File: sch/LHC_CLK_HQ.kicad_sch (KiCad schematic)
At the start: 1 part, among them U2 Si5395

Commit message: sfp+ sheet
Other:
- company: (none) -> Karlsruhe Institute of Technology (KIT)
- title: (none) -> ATCA Simple Loopback HUB
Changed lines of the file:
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@@
 (kicad_sch (version 20230121) (generator eeschema)
   (paper "A4")
+  (title_block
+    (title "ATCA Simple Loopback HUB")
+    (date "2023-09-12")
+    (rev "1.0")
+    (company "Karlsruhe Institute of Technology (KIT)")
+    (comment 1 "Institute for Data Processing and Electronics (IPE)")
+    (comment 2 "Luis Ardila")
+    (comment 3 "IPE-380-06")
+    (comment 4 "Licensed under CERN-OHL-P-2.0")
+  )
   (bus_entry (at 208.28 100.33) (size 2.54 -2.54)
     (stroke (width 0) (type default))

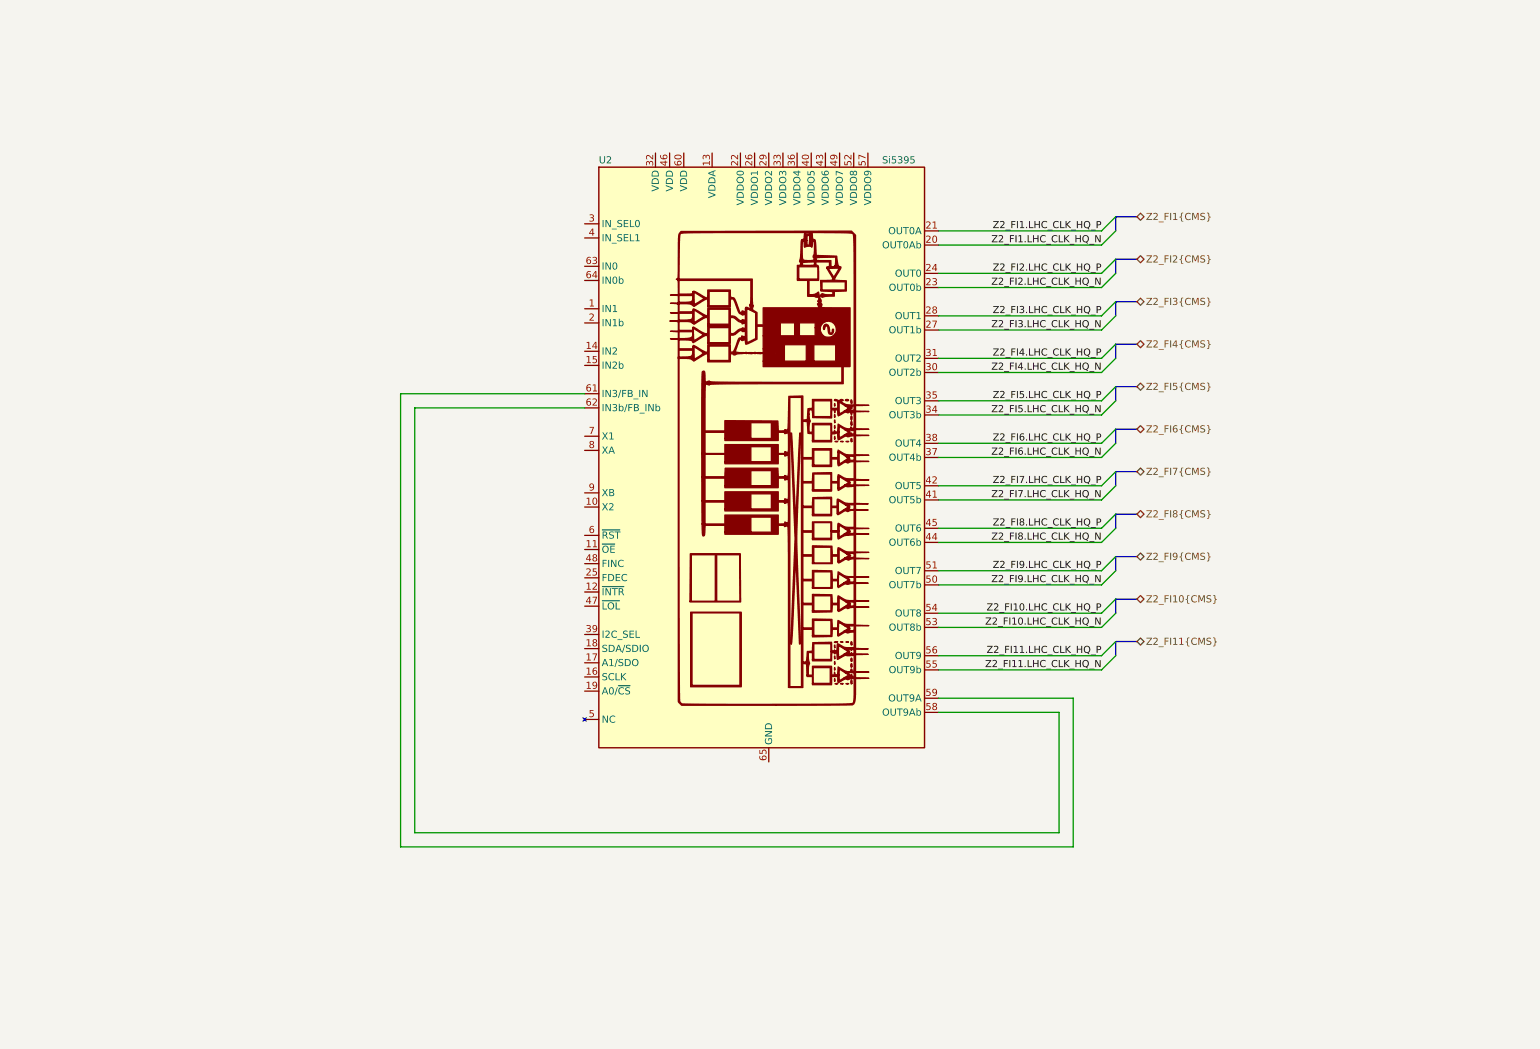
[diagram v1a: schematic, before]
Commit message: work on sc pll and pll sheet
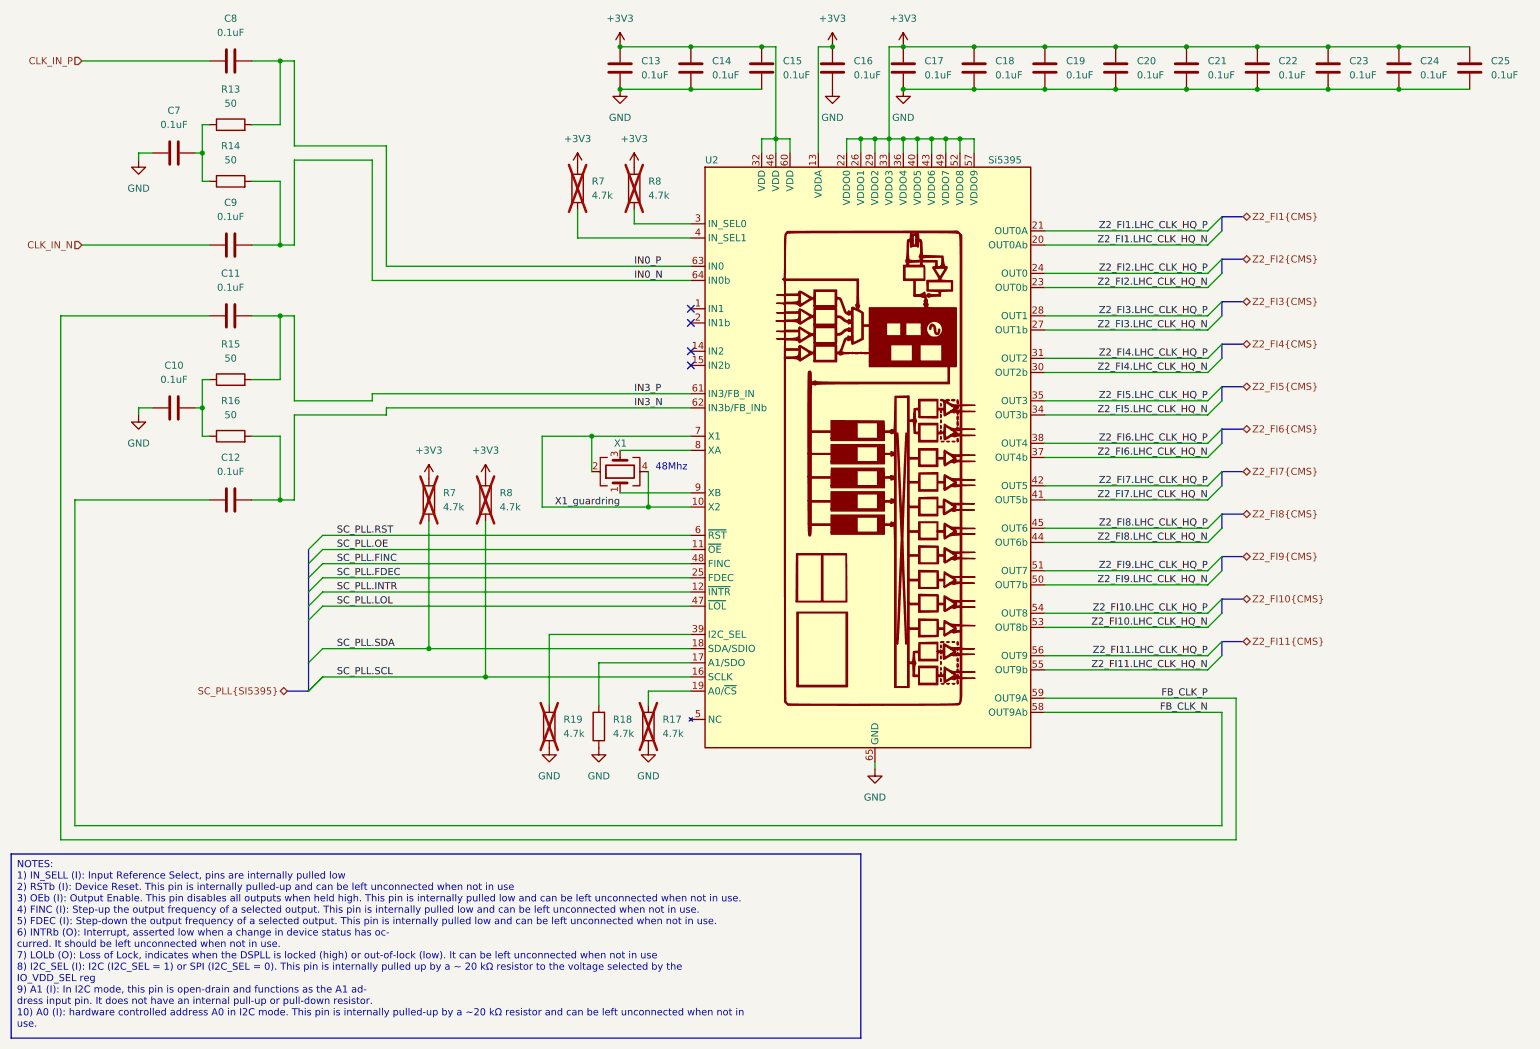
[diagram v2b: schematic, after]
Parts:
- added C10, C11, C12, C13, C14, C15, C16, C17, C18, C19, C20, C21, C22, C23, C24, C25, C7, C8, C9: 0.1uF, Capacitor_SMD:C_0402_1005Metric, symbol Device:C
- added R13, R14, R15, R16: 50, Resistor_SMD:R_0402_1005Metric, symbol Device:R
- added R17, R18, R19, R7 (x2), R8 (x2): 4.7k, Resistor_SMD:R_0402_1005Metric, symbol Device:R
- added X1: CX3225SB, Crystal:Crystal_SMD_3225-4Pin_3.2x2.5mm, symbol Device:Crystal_GND24
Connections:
- net X1_guardring: now reaches U2.10 (X2)
- net X1_guardring: now also U2.7 (X1), X1.2, X1.4
- net SC_PLL.OE: now reaches U2.11 (~{OE})
- net SC_PLL.INTR: now reaches U2.12 (~{INTR})
- net +3V3: now reaches U2.13 (VDDA)
- net +3V3: now also U2.22 (VDDO0), U2.26 (VDDO1), U2.29 (VDDO2), U2.32 (VDD), U2.33 (VDDO3), U2.36 (VDDO4), U2.40 (VDDO5), U2.43 (VDDO6), U2.46 (VDD), U2.49 (VDDO7), U2.52 (VDDO8), U2.57 (VDDO9), U2.60 (VDD), C13.2, C14.2, C15.2, C16.2, C17.2, C18.2, C19.2, C20.2, C21.2, C22.2, C23.2, C24.2, C25.2, R7.1, R7.1, R8.1, R8.1
- net SC_PLL.SCL: now reaches U2.16 (SCLK)
- net SC_PLL.SCL: now also R8.2
- net at U2.17 (A1/SDO): now also R18.2
- net SC_PLL.SDA: now reaches U2.18 (SDA/SDIO)
- net SC_PLL.SDA: now also R7.2
- net at U2.19 (A0/~{CS}): now also R17.2
- net SC_PLL.FDEC: now reaches U2.25 (FDEC)
- net at U2.3 (IN_SEL0): now also R8.2
- net at U2.39 (I2C_SEL): now also R19.2
- net at U2.4 (IN_SEL1): now also R7.2
- net SC_PLL.LOL: now reaches U2.47 (~{LOL})
- net SC_PLL.FINC: now reaches U2.48 (FINC)
- net FB_CLK_N: now reaches U2.58 (OUT9Ab)
- net FB_CLK_N: now also C12.1; no longer U2.62 (IN3b/FB_INb)
- net FB_CLK_P: now reaches U2.59 (OUT9A)
- net FB_CLK_P: now also C11.1; no longer U2.61 (IN3/FB_IN)
- net SC_PLL.RST: now reaches U2.6 (~{RST})
- net IN0_P: now reaches U2.63 (IN0)
- net IN0_P: now also C8.2, R13.2
- net IN0_N: now reaches U2.64 (IN0b)
- net IN0_N: now also C9.2, R14.2
- net GND: now reaches U2.65 (GND)
- net GND: now also C10.1, C13.1, C14.1, C15.1, C16.1, C17.1, C18.1, C19.1, C20.1, C21.1, C22.1, C23.1, C24.1, C25.1, C7.1, R17.1, R18.1, R19.1
- net at U2.8 (XA): now also X1.3
- net at U2.9 (XB): now also X1.1
- new net: C10.2, R15.1, R16.1
- new net: C7.2, R13.1, R14.1
- new net CLK_IN_N: C9.1
- new net CLK_IN_P: C8.1
- new net IN3_N: C12.2, R16.2, U2.62 (IN3b/FB_INb)
- new net IN3_P: C11.2, R15.2, U2.61 (IN3/FB_IN)
- no-connect marks 0 -> 4
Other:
- note added: "48Mhz"

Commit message: sch work
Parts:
- removed R7, R8: 4.7k, Resistor_SMD:R_0402_1005Metric, symbol Device:R
- added FB1: FerriteBead, Inductor_SMD:L_0603_1608Metric, symbol Device:FerriteBead
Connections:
- net +3V3: now also FB1.1; no longer C13.2, C14.2, C15.2, C16.2, U2.13 (VDDA), U2.32 (VDD), U2.46 (VDD), U2.60 (VDD)
- new net +1V8: C13.2, C14.2, C15.2, U2.32 (VDD), U2.46 (VDD), U2.60 (VDD)
- new net +VDDA: C16.2, FB1.2, U2.13 (VDDA)
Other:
- note added: "I2C Address = 8'b1101_001X, 8'hD2, 7'h69"

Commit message: before sch review
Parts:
- R17, R19, R7, R8: now left out of the parts list
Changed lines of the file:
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@@
   )
   (symbol (lib_id "Device:R") (at 114.3 44.45 0) (unit 1)
-    (in_bom yes) (on_board yes) (dnp yes) (fields_autoplaced)
+    (in_bom no) (on_board yes) (dnp yes) (fields_autoplaced)
     (property "Reference" "R7" (at 116.84 43.18 0)
       (effects (font (size 1.27 1.27)) (justify left))
@@
   )
   (symbol (lib_id "Device:R") (at 127 140.97 180) (unit 1)
-    (in_bom yes) (on_board yes) (dnp yes) (fields_autoplaced)
+    (in_bom no) (on_board yes) (dnp yes) (fields_autoplaced)
     (property "Reference" "R17" (at 129.54 139.7 0)
       (effects (font (size 1.27 1.27)) (justify right))
@@
   )
   (symbol (lib_id "Device:R") (at 124.46 44.45 0) (unit 1)
-    (in_bom yes) (on_board yes) (dnp yes) (fields_autoplaced)
+    (in_bom no) (on_board yes) (dnp yes) (fields_autoplaced)
     (property "Reference" "R8" (at 127 43.18 0)
       (effects (font (size 1.27 1.27)) (justify left))
@@
   )
   (symbol (lib_id "Device:R") (at 109.22 140.97 180) (unit 1)
-    (in_bom yes) (on_board yes) (dnp yes) (fields_autoplaced)
+    (in_bom no) (on_board yes) (dnp yes) (fields_autoplaced)
     (property "Reference" "R19" (at 111.76 139.7 0)
       (effects (font (size 1.27 1.27)) (justify right))

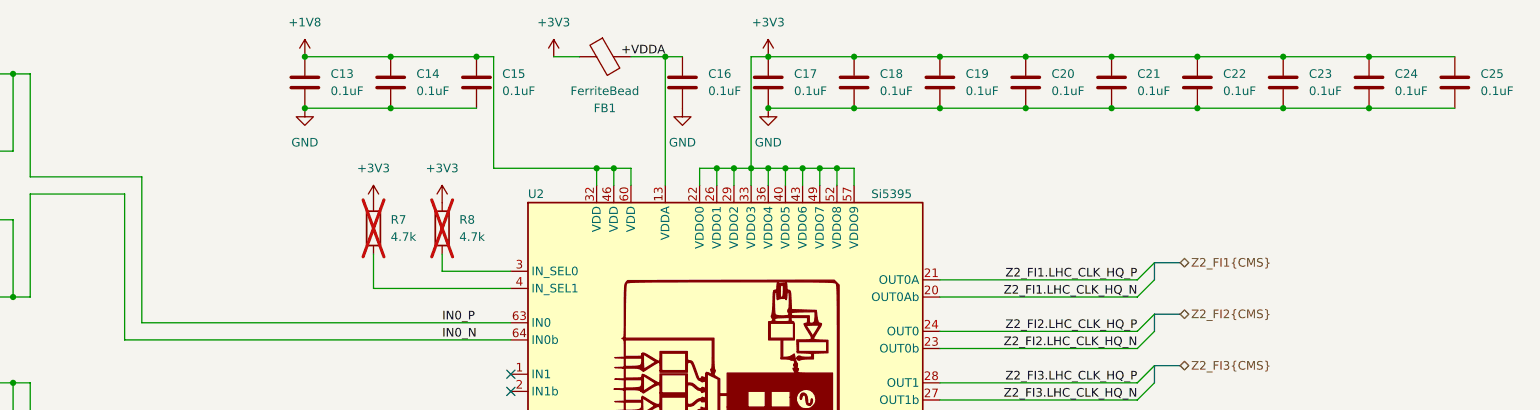
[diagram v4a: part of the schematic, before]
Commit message: started changes from review
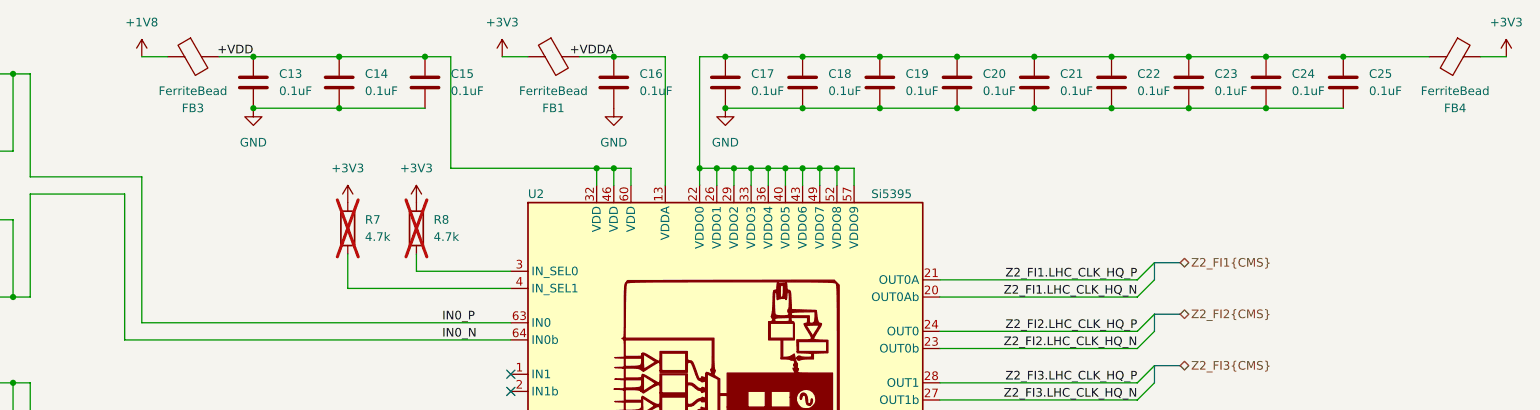
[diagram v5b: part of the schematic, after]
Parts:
- added FB3, FB4: FerriteBead, Inductor_SMD:L_0603_1608Metric, symbol Device:FerriteBead
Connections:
- net +1V8: now also FB3.1; no longer C13.2, C14.2, C15.2, U2.32 (VDD), U2.46 (VDD), U2.60 (VDD)
- net +3V3: now also FB4.1; no longer C17.2, C18.2, C19.2, C20.2, C21.2, C22.2, C23.2, C24.2, C25.2, U2.22 (VDDO0), U2.26 (VDDO1), U2.29 (VDDO2), U2.33 (VDDO3), U2.36 (VDDO4), U2.40 (VDDO5), U2.43 (VDDO6), U2.49 (VDDO7), U2.52 (VDDO8), U2.57 (VDDO9)
- new net: C17.2, C18.2, C19.2, C20.2, C21.2, C22.2, C23.2, C24.2, C25.2, FB4.2, U2.22 (VDDO0), U2.26 (VDDO1), U2.29 (VDDO2), U2.33 (VDDO3), U2.36 (VDDO4), U2.40 (VDDO5), U2.43 (VDDO6), U2.49 (VDDO7), U2.52 (VDDO8), U2.57 (VDDO9)
- new net +VDD: C13.2, C14.2, C15.2, FB3.2, U2.32 (VDD), U2.46 (VDD), U2.60 (VDD)
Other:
- moved on the sheet: R7, R8

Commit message: starting doing stackup calculations
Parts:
- C13, C14, C15, C16: value 0.1uF -> 1uF
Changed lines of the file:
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@@
       (effects (font (size 1.27 1.27)) (justify right))
     )
-    (property "Value" "0.1uF" (at 113.03 24.13 0)
+    (property "Value" "1uF" (at 113.03 24.13 0)
       (effects (font (size 1.27 1.27)) (justify right))
     )
@@
       (effects (font (size 1.27 1.27)) (justify right))
     )
-    (property "Value" "0.1uF" (at 100.33 24.13 0)
+    (property "Value" "1uF" (at 100.33 24.13 0)
       (effects (font (size 1.27 1.27)) (justify right))
     )
@@
       (effects (font (size 1.27 1.27)) (justify right))
     )
-    (property "Value" "0.1uF" (at 125.73 24.13 0)
+    (property "Value" "1uF" (at 125.73 24.13 0)
       (effects (font (size 1.27 1.27)) (justify right))
     )
@@
       (effects (font (size 1.27 1.27)) (justify right))
     )
-    (property "Value" "0.1uF" (at 153.67 24.13 0)
-      (effects (font (size 1.27 1.27)) (justify right))
-    )
+    (property "Value" "1uF" (at 153.67 24.13 0)
+      (effects (font (size 1.27 1.27)) (justify right))
+    )

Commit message: update to v8
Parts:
- renumbered C7 to C26, C10 to C27, C8 to C28, C9 to C29, C11 to C30, C12 to C31, C13 to C32, C14 to C33, C15 to C34, C16 to C35, C17 to C36, C18 to C37, C19 to C38, C20 to C39, C21 to C40, C22 to C41, C23 to C42, C24 to C43, C25 to C44, FB3 to FB2, FB1 to FB5, FB4 to FB6, R13 to R24, R14 to R25, R15 to R26, R16 to R27, R19 to R30, R7 to R31, R18 to R32, R8 to R33, R17 to R34, X1 to X2

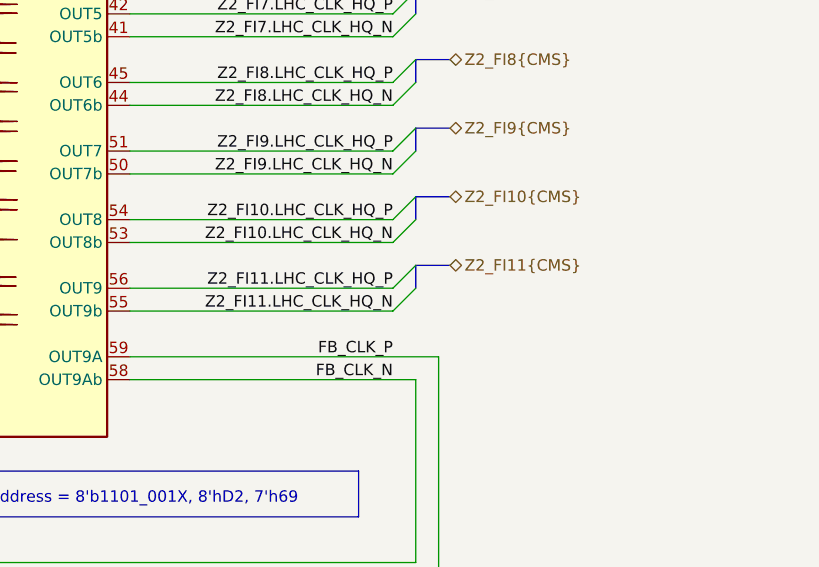
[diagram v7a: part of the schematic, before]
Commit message: added loop between plls and monitoring sma at the second stage pll
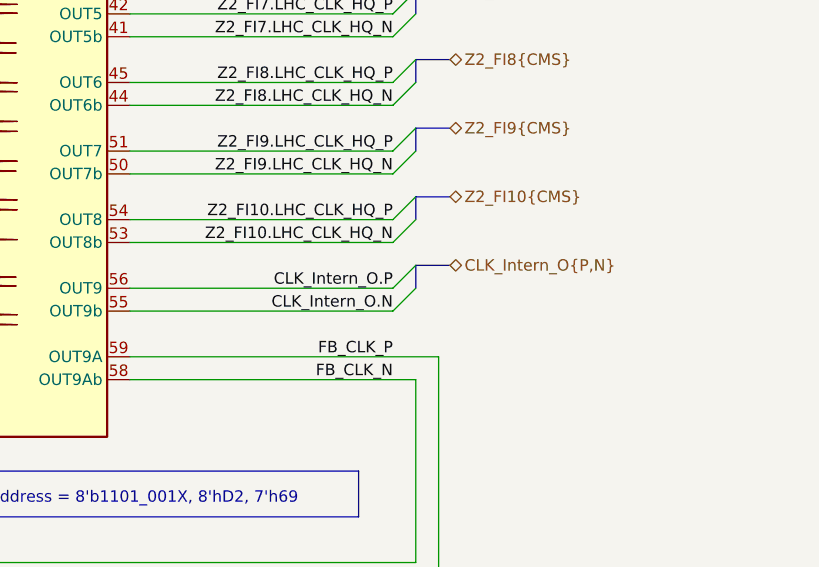
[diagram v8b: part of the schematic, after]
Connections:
- net Z2_FI11.LHC_CLK_HQ_N renamed CLK_Intern_O.N
- net Z2_FI11.LHC_CLK_HQ_P renamed CLK_Intern_O.P
